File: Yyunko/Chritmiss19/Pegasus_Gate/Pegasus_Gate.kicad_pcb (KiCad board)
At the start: 2 copper layers, 68.2 x 67.6 mm, 27 parts, among them U1 WS2811

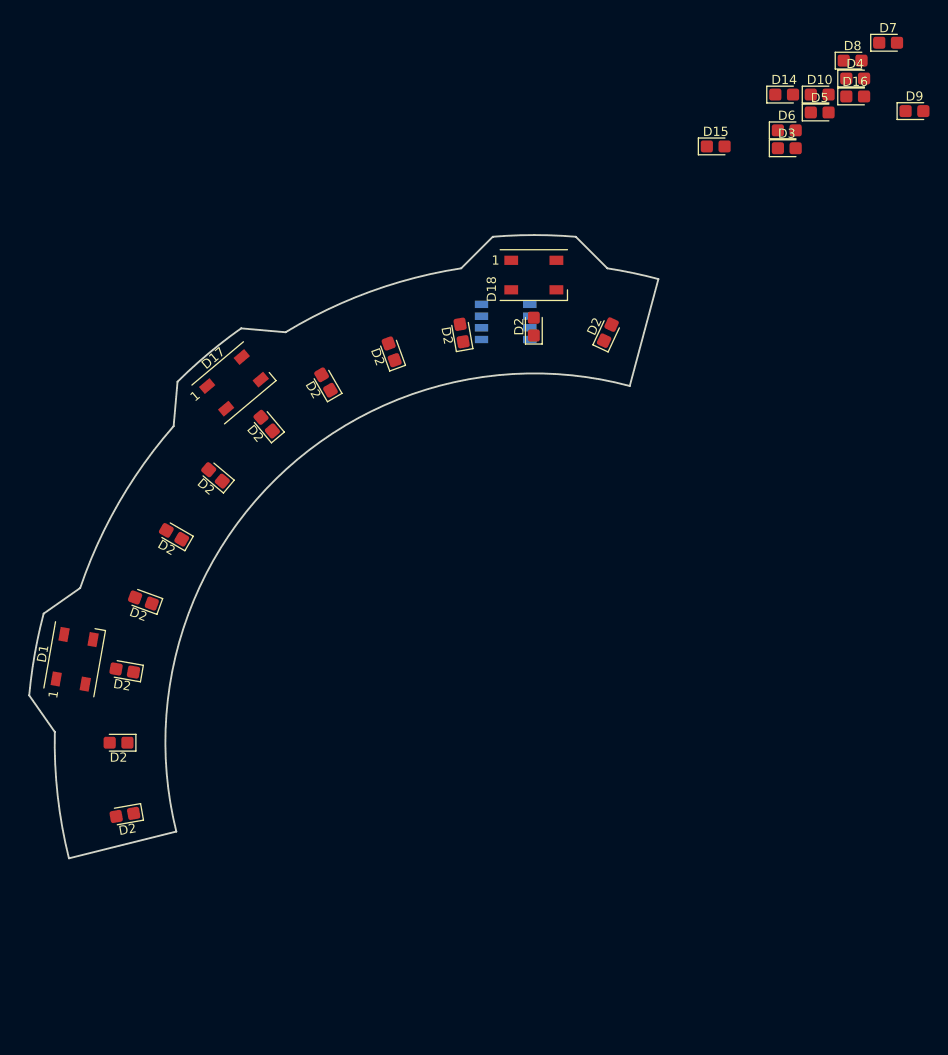
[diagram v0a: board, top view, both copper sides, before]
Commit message: Added sidemount LED footprint
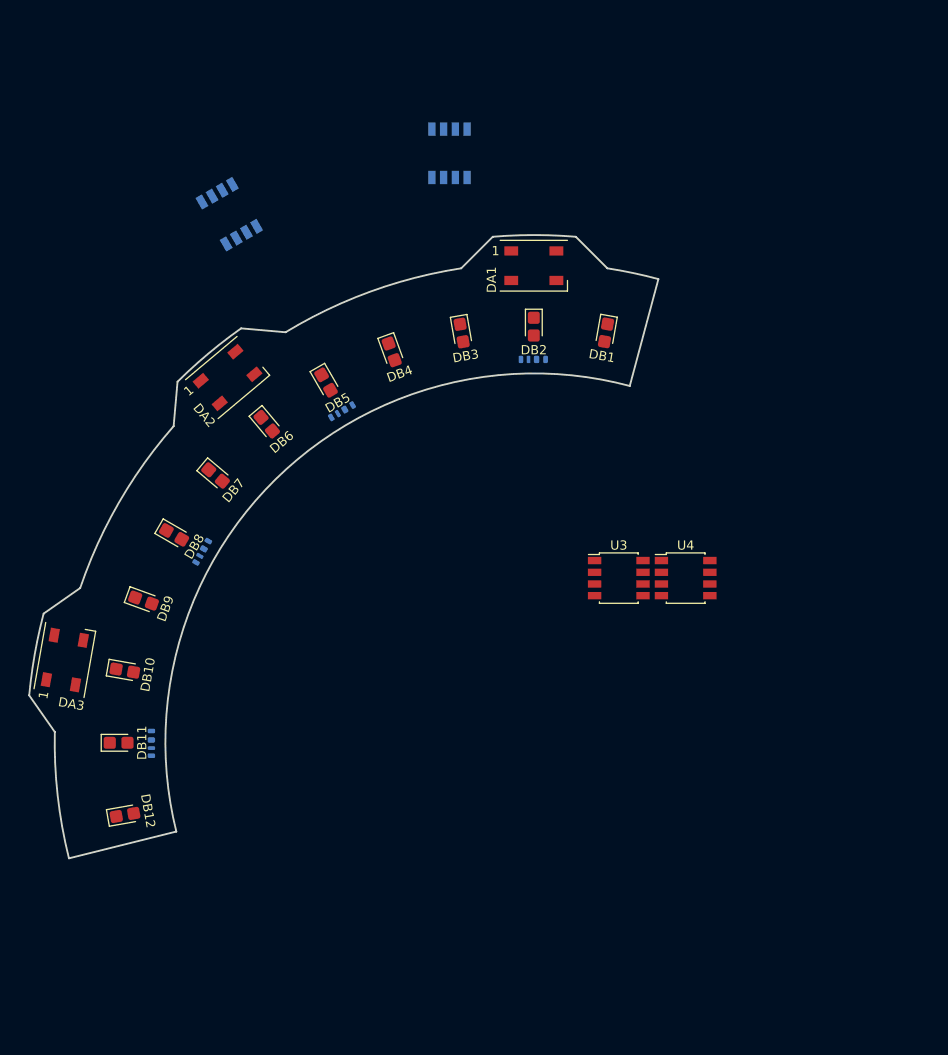
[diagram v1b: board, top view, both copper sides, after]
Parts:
- removed D1, D17, D18: WS2812B, LED_SMD:LED_WS2812B_PLCC4_5.0x5.0mm_P3.2mm
- removed D10, D14, D15, D16, D2 (x12), D3, D4, D5, D6, D7, D8, D9: LED, LED_SMD:LED_0805_2012Metric_Castellated
- added DA1: WS2812B, LED_SMD:LED_WS2812B_PLCC4_5.0x5.0mm_P3.2mm, F.Cu at (148.3, 64.0)
- added DA2: WS2812B, LED_SMD:LED_WS2812B_PLCC4_5.0x5.0mm_P3.2mm, F.Cu at (115.1, 76.1)
- added DA3: WS2812B, LED_SMD:LED_WS2812B_PLCC4_5.0x5.0mm_P3.2mm, F.Cu at (97.5, 106.8)
- added DB1: LED, LED_SMD:LED_0805_2012Metric_Castellated, F.Cu at (156.2, 71.3)
- added DB10: LED, LED_SMD:LED_0805_2012Metric_Castellated, F.Cu at (104.0, 107.9)
- added DB11: LED, LED_SMD:LED_0805_2012Metric_Castellated, F.Cu at (103.3, 115.7)
- added DB12: LED, LED_SMD:LED_0805_2012Metric_Castellated, F.Cu at (104.0, 123.6)
- added DB2: LED, LED_SMD:LED_0805_2012Metric_Castellated, F.Cu at (148.3, 70.6)
- added DB3: LED, LED_SMD:LED_0805_2012Metric_Castellated, F.Cu at (140.5, 71.3)
- added DB4: LED, LED_SMD:LED_0805_2012Metric_Castellated, F.Cu at (132.9, 73.3)
- added DB5: LED, LED_SMD:LED_0805_2012Metric_Castellated, F.Cu at (125.8, 76.7)
- added DB6: LED, LED_SMD:LED_0805_2012Metric_Castellated, F.Cu at (119.4, 81.2)
- added DB7: LED, LED_SMD:LED_0805_2012Metric_Castellated, F.Cu at (113.8, 86.8)
- added DB8: LED, LED_SMD:LED_0805_2012Metric_Castellated, F.Cu at (109.3, 93.2)
- added DB9: LED, LED_SMD:LED_0805_2012Metric_Castellated, F.Cu at (106.0, 100.3)
- added DC1: WS2812B, Local:IN-PI42TAS, B.Cu at (148.3, 74.2)
- added DC2: WS2812B, Local:IN-PI42TAS, B.Cu at (127.6, 79.8)
- added DC3: WS2812B, Local:IN-PI42TAS, B.Cu at (112.4, 95.0)
- added DC4: WS2812B, Local:IN-PI42TAS, B.Cu at (106.9, 115.7)
- added U2: WS2811, Package_SO:SSOP-8_3.95x5.21x3.27mm_P1.27mm, B.Cu at (115.3, 58.4)
- added U3: WS2811, Package_SO:SSOP-8_3.95x5.21x3.27mm_P1.27mm, F.Cu at (157.5, 97.9)
- added U4: WS2811, Package_SO:SSOP-8_3.95x5.21x3.27mm_P1.27mm, F.Cu at (164.8, 97.9)
- moved U1 19.3 mm to (139.2, 51.8), turned to 90 degrees

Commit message: Almost sorted all secs out
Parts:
- added C1: 10uF, Capacitor_SMD:C_0805_2012Metric, B.Cu at (154.4, 67.6)
- added C2: 100nF, Capacitor_SMD:C_0805_2012Metric, B.Cu at (152.4, 67.6)
- added C3: 10uF, Capacitor_SMD:C_0805_2012Metric, B.Cu at (129.6, 71.0)
- added C4: 100nF, Capacitor_SMD:C_0805_2012Metric, B.Cu at (127.8, 72.0)
- added C5: 10uF, Capacitor_SMD:C_0805_2012Metric, B.Cu at (109.7, 86.4)
- added C6: 100nF, Capacitor_SMD:C_0805_2012Metric, B.Cu at (108.7, 88.1)
- added C7: 10uF, Capacitor_SMD:C_0805_2012Metric, B.Cu at (100.3, 109.6)
- added C8: 100nF, Capacitor_SMD:C_0805_2012Metric, B.Cu at (100.3, 111.7)
- added DD1: WS2812B, Local:IN-PI42TAS, B.Cu at (148.4, 62.1)
- added DD2: WS2812B, Local:IN-PI42TAS, B.Cu at (113.9, 74.6)
- added DD3: WS2812B, Local:IN-PI42TAS, B.Cu at (95.6, 106.4)
- added J1: Conn_01x03_Female, Connector_PinHeader_2.00mm:PinHeader_1x03_P2.00mm_Vertical, F.Cu at (160.8, 69.3)
- added J2: Conn_01x03_Female, Connector_PinHeader_2.00mm:PinHeader_1x03_P2.00mm_Vertical, F.Cu at (102.1, 127.3)
- added JP1: Jumper_NC_Small, Jumper:SolderJumper-2_P1.3mm_Bridged_Pad1.0x1.5mm, F.Cu at (173.8, 69.0)
- U3, U4: moved to B.Cu
- moved U1 74.0 mm to (101.8, 115.7), turned to 180 degrees
- moved U3 39.5 mm to (125.0, 75.4), turned to 120 degrees
- moved U2 34.8 mm to (108.0, 92.4), turned to 150 degrees
- moved U4 33.2 mm to (148.3, 69.1), turned to 90 degrees
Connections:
- DA1 pad 1: Net-(DA1-Pad1) -> +5V
- DA1 pad 3: Net-(DA1-Pad3) -> GND
- DA1 pad 4: Net-(DA1-Pad4) -> /IN_A
- DA2 pad 1: Net-(DA2-Pad1) -> +5V
- DA2 pad 3: Net-(DA2-Pad3) -> GND
- DA3 pad 1: Net-(DA3-Pad1) -> +5V
- DA3 pad 3: Net-(DA3-Pad3) -> GND
- DC1 pad 1: Net-(DC2-Pad1) -> Net-(DC1-Pad1)
- DC1 pad 2: Net-(DC2-Pad2) -> Net-(DC1-Pad2)
- DC1 pad 3: Net-(DC2-Pad3) -> Net-(DC1-Pad3)
- DC1 pad 4: Net-(DC2-Pad4) -> /IN_C
- DC2 pad 4: Net-(DC2-Pad4) -> Net-(DC1-Pad2)
- DC3 pad 1: Net-(DC2-Pad1) -> Net-(DC3-Pad1)
- DC3 pad 2: Net-(DC2-Pad2) -> Net-(DC3-Pad2)
- DC3 pad 3: Net-(DC2-Pad3) -> Net-(DC3-Pad3)
- DC3 pad 4: Net-(DC2-Pad4) -> Net-(DC2-Pad2)
- DC4 pad 1: Net-(DC2-Pad1) -> Net-(DC4-Pad1)
- DC4 pad 2: Net-(DC2-Pad2) -> /SIG_OUT
- DC4 pad 3: Net-(DC2-Pad3) -> Net-(DC4-Pad3)
- DC4 pad 4: Net-(DC2-Pad4) -> Net-(DC3-Pad2)
- U1 pad 1: Net-(DB1-Pad1) -> Net-(DB10-Pad1)
- U1 pad 2: Net-(DB2-Pad1) -> Net-(DB11-Pad1)
- U1 pad 3: Net-(DB3-Pad1) -> Net-(DB12-Pad1)
- U1 pad 4: Net-(U1-Pad4) -> GND
- U1 pad 6: Net-(U1-Pad6) -> /IN_B
- U1 pad 8: Net-(U1-Pad8) -> +5V
- U2 pad 1: Net-(DB4-Pad1) -> Net-(DB7-Pad1)
- U2 pad 2: Net-(DB5-Pad1) -> Net-(DB8-Pad1)
- U2 pad 3: Net-(DB6-Pad1) -> Net-(DB9-Pad1)
- U2 pad 4: Net-(U2-Pad4) -> GND
- U2 pad 6: Net-(U2-Pad6) -> Net-(U1-Pad5)
- U2 pad 8: Net-(U2-Pad8) -> +5V
- U3 pad 1: Net-(DB7-Pad1) -> Net-(DB4-Pad1)
- U3 pad 2: Net-(DB8-Pad1) -> Net-(DB5-Pad1)
- U3 pad 3: Net-(DB9-Pad1) -> Net-(DB6-Pad1)
- U3 pad 4: Net-(U3-Pad4) -> GND
- U3 pad 6: Net-(U3-Pad6) -> Net-(U2-Pad5)
- U3 pad 8: Net-(U3-Pad8) -> +5V
- U4 pad 1: Net-(DB10-Pad1) -> Net-(DB1-Pad1)
- U4 pad 2: Net-(DB11-Pad1) -> Net-(DB2-Pad1)
- U4 pad 3: Net-(DB12-Pad1) -> Net-(DB3-Pad1)
- U4 pad 4: Net-(U4-Pad4) -> GND
- U4 pad 5: Net-(U4-Pad5) -> /IN_C
- U4 pad 6: Net-(U4-Pad6) -> Net-(U3-Pad5)
- U4 pad 8: Net-(U4-Pad8) -> +5V
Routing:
- net +5V: track 0.00 -> 17.9 mm
- added copper zone on F.Cu, net +5V
- added copper zone on B.Cu, net GND

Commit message: Continue work on PCB and Schematic
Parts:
- moved JP1 10.2 mm to (164.2, 72.5)
- moved C1 8.05 mm to (160.3, 73.1)
- moved C4 8.05 mm to (133.7, 77.5)
- moved C7 8.05 mm to (106.2, 115.1)
- moved C8 8.05 mm to (106.2, 117.1)
- moved DA3 8.05 mm to (103.4, 112.2)
- moved DB10 8.05 mm to (109.9, 113.4)
- moved DB12 8.05 mm to (109.9, 129.0)
- moved DB8 8.05 mm to (115.2, 98.7)
- moved DC2 8.05 mm to (133.5, 85.2)
- moved DD3 8.05 mm to (101.5, 111.9)
- moved U1 8.05 mm to (107.7, 121.2)
- moved C6 8.05 mm to (114.6, 93.6)
- moved DB7 8.05 mm to (119.7, 92.2)
- moved DD2 8.05 mm to (119.8, 80.1)
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
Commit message: Continue woork
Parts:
- moved JP1 1.51 mm to (162.8, 73.0), turned to 80 degrees
- moved J2 0.81 mm to (107.8, 132.0), turned to 104 degrees
- moved J1 0.69 mm to (166.0, 74.8)
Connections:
- DC1 pad 1: Net-(DC1-Pad1) -> +5V
- DC1 pad 3: Net-(DC1-Pad3) -> GND
- DC2 pad 1: Net-(DC2-Pad1) -> +5V
- DC2 pad 3: Net-(DC2-Pad3) -> GND
- DC3 pad 1: Net-(DC3-Pad1) -> +5V
- DC3 pad 3: Net-(DC3-Pad3) -> GND
- DC4 pad 1: Net-(DC4-Pad1) -> +5V
- DC4 pad 3: Net-(DC4-Pad3) -> GND
- J2 pad 1: Net-(J2-Pad1) -> +5V
- J2 pad 3: Net-(J2-Pad3) -> GND
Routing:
- net Net-(DA3-Pad4): track 0.00 -> 37.0 mm, vias 0 -> 1
- net Net-(DA2-Pad4): track 0.00 -> 36.7 mm, vias 0 -> 1
- net Net-(U1-Pad5): track 0.00 -> 29.5 mm, vias 0 -> 2
- net Net-(U3-Pad5): track 0.00 -> 29.3 mm, vias 0 -> 2
- net Net-(U2-Pad5): track 0.00 -> 28.1 mm, vias 0 -> 2
- net Net-(DC1-Pad2): track 0.00 -> 22.0 mm
- net Net-(DC3-Pad2): track 0.00 -> 21.6 mm
- net Net-(DC2-Pad2): track 0.00 -> 20.9 mm
- net /IN_B: track 0.00 -> 12.5 mm
- net /IN_C: track 0.00 -> 11.9 mm
- net /SIG_OUT: track 0.00 -> 11.2 mm
- net Net-(DB9-Pad1): track 0.00 -> 9.24 mm, vias 0 -> 1
- net Net-(DB6-Pad1): track 0.00 -> 8.83 mm, vias 0 -> 1
- net Net-(DB12-Pad1): track 0.00 -> 8.59 mm, vias 0 -> 1
- net Net-(DB3-Pad1): track 0.00 -> 8.34 mm, vias 0 -> 1
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
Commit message: Begin work on assigning part nums
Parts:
- DA1, DA2, DA3: value WS2812B -> BL-HRGB32K-3-TRBCT-ND
- DB1, DB10, DB11, DB12, DB2, DB3, DB4, DB5, DB6, DB7, DB8, DB9: value LED -> 754-1437-6-ND
- DC1, DC2, DC3, DC4, DD1, DD2, DD3: value WS2812B -> 1830-1206-1-ND
- U4: value WS2811 -> 1528-1537-ND
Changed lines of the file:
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@@
       (effects (font (size 1 1) (thickness 0.15)) (justify mirror))
     )
-    (fp_text value WS2812B (at -3.556 -6.604 260) (layer B.Fab)
+    (fp_text value 1830-1206-1-ND (at -3.556 -6.604 260) (layer B.Fab)
       (effects (font (size 1 1) (thickness 0.15)) (justify mirror))
     )
@@
       (effects (font (size 1 1) (thickness 0.15)) (justify mirror))
     )
-    (fp_text value WS2812B (at -3.556 -6.604 220) (layer B.Fab)
+    (fp_text value 1830-1206-1-ND (at -3.556 -6.604 220) (layer B.Fab)
       (effects (font (size 1 1) (thickness 0.15)) (justify mirror))
     )
@@
       (effects (font (size 1 1) (thickness 0.15)) (justify mirror))
     )
-    (fp_text value WS2812B (at -3.556 -6.604 180) (layer B.Fab)
+    (fp_text value 1830-1206-1-ND (at -3.556 -6.604 180) (layer B.Fab)
       (effects (font (size 1 1) (thickness 0.15)) (justify mirror))
     )
@@
       (effects (font (size 1 1) (thickness 0.15)) (justify mirror))
     )
-    (fp_text value WS2812B (at -3.556 -6.604 90) (layer B.Fab)
+    (fp_text value 1830-1206-1-ND (at -3.556 -6.604 90) (layer B.Fab)
       (effects (font (size 1 1) (thickness 0.15)) (justify mirror))
     )
@@
       (effects (font (size 1 1) (thickness 0.15)) (justify mirror))
     )
-    (fp_text value WS2812B (at -3.556 -6.604 60) (layer B.Fab)
+    (fp_text value 1830-1206-1-ND (at -3.556 -6.604 60) (layer B.Fab)
       (effects (font (size 1 1) (thickness 0.15)) (justify mirror))
     )
@@
       (effects (font (size 1 1) (thickness 0.15)) (justify mirror))
     )
-    (fp_text value WS2812B (at -3.556 -6.604 30) (layer B.Fab)
+    (fp_text value 1830-1206-1-ND (at -3.556 -6.604 30) (layer B.Fab)
       (effects (font (size 1 1) (thickness 0.15)) (justify mirror))
     )
@@
       (effects (font (size 1 1) (thickness 0.15)) (justify mirror))
     )
-    (fp_text value WS2812B (at -3.556 -6.604) (layer B.Fab)
+    (fp_text value 1830-1206-1-ND (at -3.556 -6.604) (layer B.Fab)
       (effects (font (size 1 1) (thickness 0.15)) (justify mirror))
     )
@@
       (effects (font (size 1 1) (thickness 0.15)) (justify mirror))
     )
-    (fp_text value WS2811 (at 0 -3.75 90) (layer B.Fab)
+    (fp_text value 1528-1537-ND (at 0 -3.75 90) (layer B.Fab)
       (effects (font (size 1 1) (thickness 0.15)) (justify mirror))
     )
@@
       (effects (font (size 1 1) (thickness 0.15)))
     )
-    (fp_text value WS2812B (at 0 4 80) (layer F.Fab)
+    (fp_text value BL-HRGB32K-3-TRBCT-ND (at 0 4 80) (layer F.Fab)
       (effects (font (size 1 1) (thickness 0.15)))
     )
@@
       (effects (font (size 1 1) (thickness 0.15)))
     )
-    (fp_text value WS2812B (at 0 4 40) (layer F.Fab)
+    (fp_text value BL-HRGB32K-3-TRBCT-ND (at 0 4 40) (layer F.Fab)
       (effects (font (size 1 1) (thickness 0.15)))
     )
@@
       (effects (font (size 1 1) (thickness 0.15)))
     )
-    (fp_text value LED (at 0 1.6 260) (layer F.Fab)
+    (fp_text value 754-1437-6-ND (at 0 1.6 260) (layer F.Fab)
       (effects (font (size 1 1) (thickness 0.15)))
     )
@@
       (effects (font (size 1 1) (thickness 0.15)))
     )
-    (fp_text value LED (at 0 1.6 10) (layer F.Fab)
+    (fp_text value 754-1437-6-ND (at 0 1.6 10) (layer F.Fab)
       (effects (font (size 1 1) (thickness 0.15)))
     )
@@
       (effects (font (size 1 1) (thickness 0.15)))
     )
-    (fp_text value LED (at 0 1.6) (layer F.Fab)
+    (fp_text value 754-1437-6-ND (at 0 1.6) (layer F.Fab)
       (effects (font (size 1 1) (thickness 0.15)))
     )
@@
       (effects (font (size 1 1) (thickness 0.15)))
     )
-    (fp_text value LED (at 0 1.6 350) (layer F.Fab)
+    (fp_text value 754-1437-6-ND (at 0 1.6 350) (layer F.Fab)
       (effects (font (size 1 1) (thickness 0.15)))
     )
@@
       (effects (font (size 1 1) (thickness 0.15)))
     )
-    (fp_text value LED (at 0 1.6 340) (layer F.Fab)
+    (fp_text value 754-1437-6-ND (at 0 1.6 340) (layer F.Fab)
       (effects (font (size 1 1) (thickness 0.15)))
     )
@@
       (effects (font (size 1 1) (thickness 0.15)))
     )
-    (fp_text value LED (at 0 1.6 330) (layer F.Fab)
+    (fp_text value 754-1437-6-ND (at 0 1.6 330) (layer F.Fab)
       (effects (font (size 1 1) (thickness 0.15)))
     )
@@
       (effects (font (size 1 1) (thickness 0.15)))
     )
-    (fp_text value LED (at 0 1.6 320) (layer F.Fab)
+    (fp_text value 754-1437-6-ND (at 0 1.6 320) (layer F.Fab)
       (effects (font (size 1 1) (thickness 0.15)))
     )
@@
       (effects (font (size 1 1) (thickness 0.15)))
     )
-    (fp_text value LED (at 0 1.6 310) (layer F.Fab)
+    (fp_text value 754-1437-6-ND (at 0 1.6 310) (layer F.Fab)
       (effects (font (size 1 1) (thickness 0.15)))
     )
@@
       (effects (font (size 1 1) (thickness 0.15)))
     )
-    (fp_text value LED (at 0 1.6 300) (layer F.Fab)
+    (fp_text value 754-1437-6-ND (at 0 1.6 300) (layer F.Fab)
       (effects (font (size 1 1) (thickness 0.15)))
     )
@@
       (effects (font (size 1 1) (thickness 0.15)))
     )
-    (fp_text value LED (at 0 1.6 290) (layer F.Fab)
+    (fp_text value 754-1437-6-ND (at 0 1.6 290) (layer F.Fab)
       (effects (font (size 1 1) (thickness 0.15)))
     )
@@
       (effects (font (size 1 1) (thickness 0.15)))
     )
-    (fp_text value LED (at 0 1.6 280) (layer F.Fab)
+    (fp_text value 754-1437-6-ND (at 0 1.6 280) (layer F.Fab)
       (effects (font (size 1 1) (thickness 0.15)))
     )
@@
       (effects (font (size 1 1) (thickness 0.15)))
     )
-    (fp_text value LED (at 0 1.6 270) (layer F.Fab)
+    (fp_text value 754-1437-6-ND (at 0 1.6 270) (layer F.Fab)
       (effects (font (size 1 1) (thickness 0.15)))
     )
@@
       (effects (font (size 1 1) (thickness 0.15)))
     )
-    (fp_text value WS2812B (at 0 4) (layer F.Fab)
+    (fp_text value BL-HRGB32K-3-TRBCT-ND (at 0 4) (layer F.Fab)
       (effects (font (size 1 1) (thickness 0.15)))
     )
@@
   (segment (start 148.0146 71.9494) (end 153.5938 71.9494) (width 0.25) (layer F.Cu) (net 3))
   (segment (start 143.002 76.962) (end 148.0146 71.9494) (width 0.25) (layer F.Cu) (net 3))
-  (via (at 123.952 81.28) (size 0.8) (drill 0.4) (layers F.Cu B.Cu) (net 29))
-  (via (at 157.226 70.739) (size 0.8) (drill 0.4) (layers F.Cu B.Cu) (net 29))
-  (via (at 105.41 110.109) (size 0.8) (drill 0.4) (layers F.Cu B.Cu) (net 29))
   (segment (start 111.58286 104.895097) (end 111.58286 102.28514) (width 0.25) (layer F.Cu) (net 5))
   (segment (start 111.005017 105.47294) (end 111.58286 104.895097) (width 0.25) (layer F.Cu) (net 5))
@@
   (segment (start 136.89067 82.296) (end 134.582315 84.604355) (width 0.25) (layer B.Cu) (net 28))
   (segment (start 140.081 82.296) (end 136.89067 82.296) (width 0.25) (layer B.Cu) (net 28))
+  (via (at 123.952 81.28) (size 0.8) (drill 0.4) (layers F.Cu B.Cu) (net 29))
+  (via (at 157.226 70.739) (size 0.8) (drill 0.4) (layers F.Cu B.Cu) (net 29))
+  (via (at 105.41 110.109) (size 0.8) (drill 0.4) (layers F.Cu B.Cu) (net 29))
   (segment (start 101.222859 110.473013) (end 100.673361 111.022511) (width 0.25) (layer B.Cu) (net 29))
   (segment (start 100.673361 111.022511) (end 100.457 112.249554) (width 0.25) (layer B.Cu) (net 29))

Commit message: Continue work on durg ring thing
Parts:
- added SYM1: SYM_Radioactive_Large, Local:DragonIcon, B.Cu at (117.2, 99.4)
- moved J1 33.2 mm to (136.9, 58.9), turned to 32 degrees
- moved J2 32.3 mm to (139.0, 140.4), turned to 151 degrees
- moved JP1 32.2 mm to (133.4, 60.0), turned to 127 degrees
- moved DD1 31.1 mm to (123.6, 62.5), turned to 227 degrees
- moved C1 30.7 mm to (131.7, 61.9), turned to 317 degrees
- moved DA1 29.8 mm to (125.0, 63.9), turned to 47 degrees
- moved DB1 29.8 mm to (135.6, 63.1), turned to 307 degrees
- moved C2 29.6 mm to (130.3, 63.3), turned to 317 degrees
- moved DB12 29.4 mm to (138.3, 136.9), turned to 57 degrees
- moved DD3 26.9 mm to (120.0, 131.4), turned to 307 degrees
- moved U4 26.6 mm to (128.7, 67.4), turned to 137 degrees
- moved U1 26.3 mm to (131.0, 133.2), turned to 227 degrees
- moved DB2 25.6 mm to (129.8, 68.4), turned to 317 degrees
- moved DA3 25.6 mm to (121.5, 130.2), turned to 127 degrees
- moved C8 25.3 mm to (127.0, 131.5), turned to 47 degrees
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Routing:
- net +5V: track 19.1 -> 21.2 mm
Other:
- board size 68.2 x 67.6 mm -> 35.6 x 89.6 mm
- board text added: "GND SIG +5V"

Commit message: Begin work on ESP32 code
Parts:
- removed JP1: Jumper_NC_Small, Jumper:SolderJumper-2_P1.3mm_Bridged_Pad1.0x1.5mm
- J1, J2: footprint Connector_PinHeader_2.00mm:PinHeader_1x03_P2.00mm_Vertical -> Connector_PinHeader_2.54mm:PinHeader_1x03_P2.54mm_Vertical
- moved J1 4.03 mm to (138.9, 62.4), turned to 212 degrees
- moved J2 0.42 mm to (138.7, 140.7)
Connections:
- J1 pad 2: Net-(J1-Pad2) -> /IN_A
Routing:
- net /IN_A: track 8.11 -> 13.5 mm
- net Net-(J1-Pad2): track 4.22 -> 0.00 mm
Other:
- board text added: "GND < SIG +5V"
- board text removed: "GND SIG +5V"
